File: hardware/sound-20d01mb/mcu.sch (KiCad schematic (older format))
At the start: 23 parts

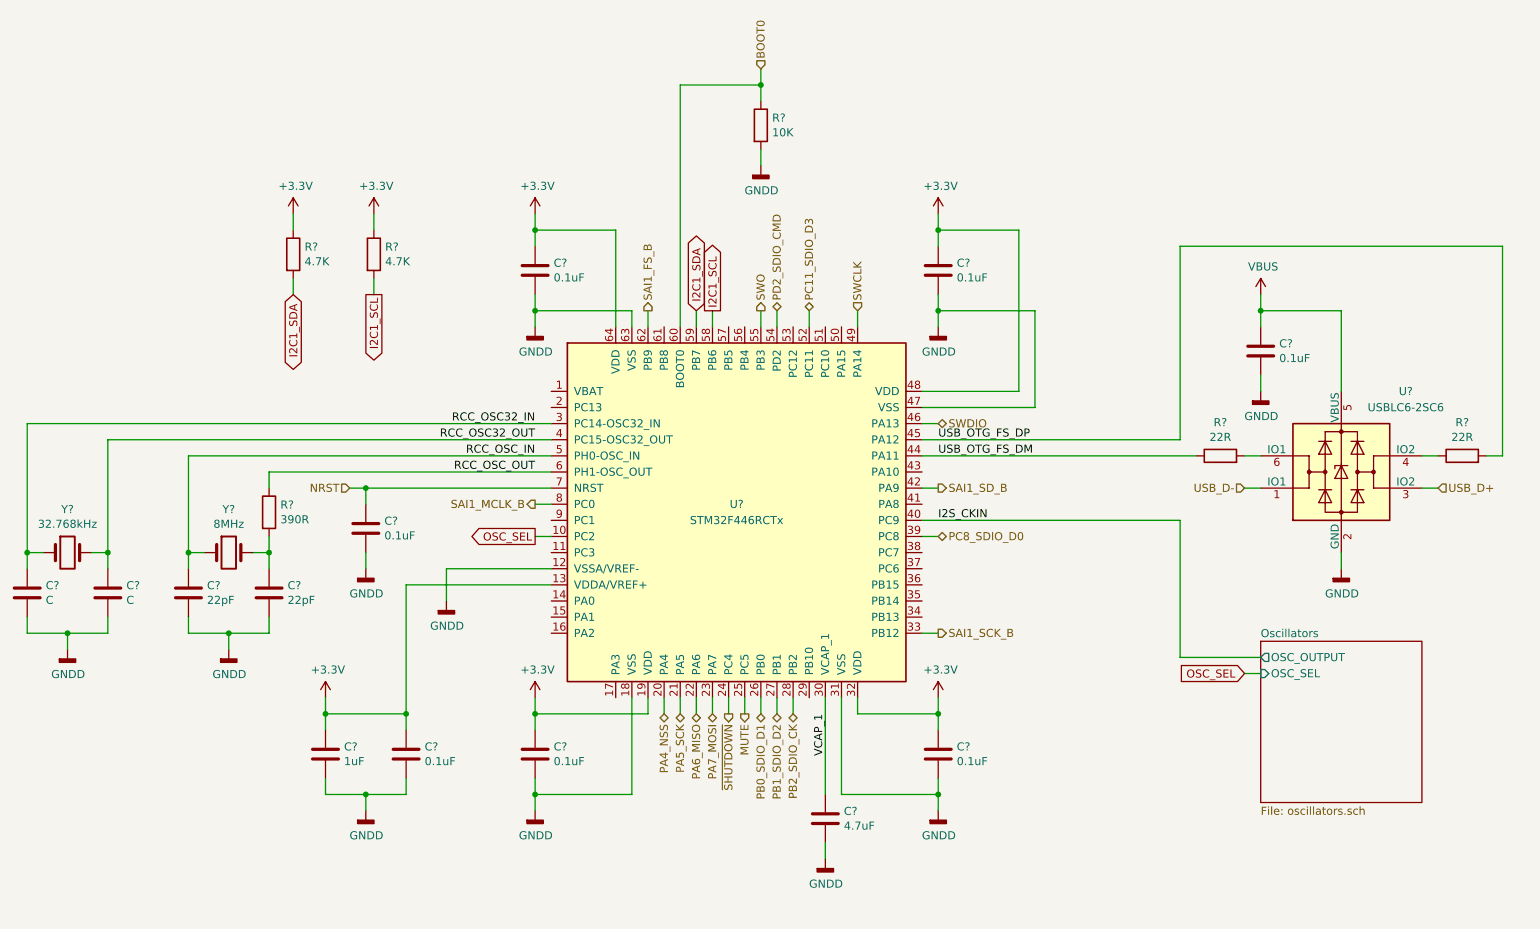
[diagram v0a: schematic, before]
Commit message: Added GPIO for MCU
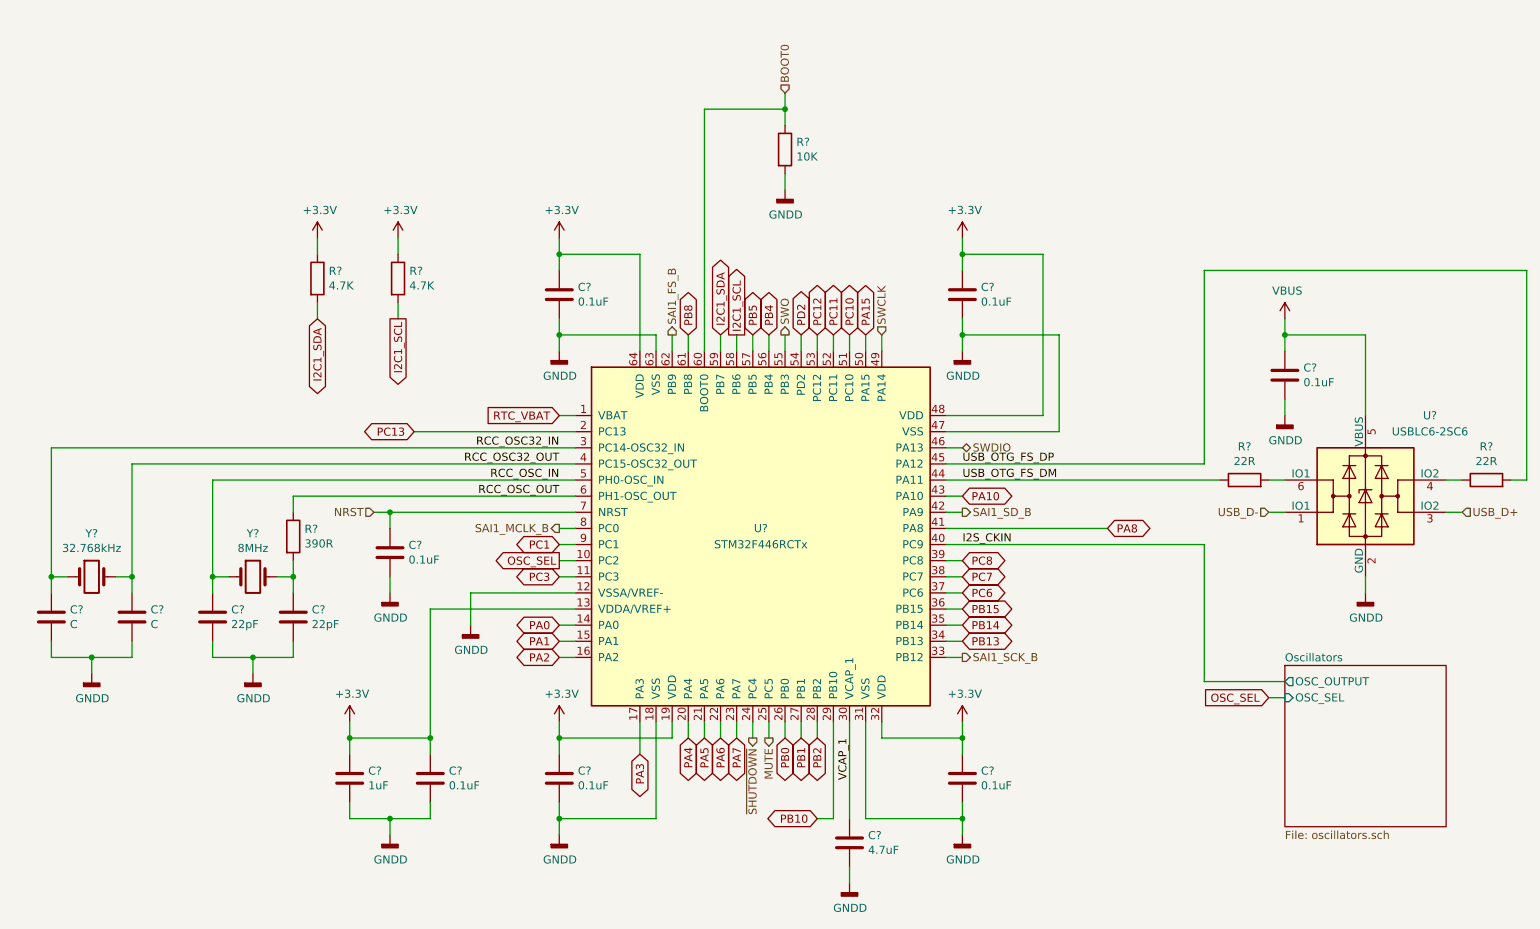
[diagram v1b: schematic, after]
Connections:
- net RTC_VBAT: now reaches U?.1 (VBAT)
- net PC3: now reaches U?.11 (PC3)
- net PA0: now reaches U?.14 (PA0)
- net PA1: now reaches U?.15 (PA1)
- net PA2: now reaches U?.16 (PA2)
- net PA3: now reaches U?.17 (PA3)
- net PC13: now reaches U?.2 (PC13)
- net PB10: now reaches U?.29 (PB10)
- net PB13: now reaches U?.34 (PB13)
- net PB14: now reaches U?.35 (PB14)
- net PB15: now reaches U?.36 (PB15)
- net PC6: now reaches U?.37 (PC6)
- net PC7: now reaches U?.38 (PC7)
- net PA8: now reaches U?.41 (PA8)
- net PA10: now reaches U?.43 (PA10)
- net PA15: now reaches U?.50 (PA15)
- net PC10: now reaches U?.51 (PC10)
- net PC12: now reaches U?.53 (PC12)
- net PB4: now reaches U?.56 (PB4)
- net PB5: now reaches U?.57 (PB5)
- net PB8: now reaches U?.61 (PB8)
- net PC1: now reaches U?.9 (PC1)
- net PA4_NSS renamed PA4
- net PA5_SCK renamed PA5
- net PA6_MISO renamed PA6
- net PA7_MOSI renamed PA7
- net PB0_SDIO_D1 renamed PB0
- net PB1_SDIO_D2 renamed PB1
- net PB2_SDIO_CK renamed PB2
- net PC11_SDIO_D3 renamed PC11
- net PC8_SDIO_D0 renamed PC8
- net PD2_SDIO_CMD renamed PD2
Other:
- moved on the sheet: C?, R?, U?, Y?

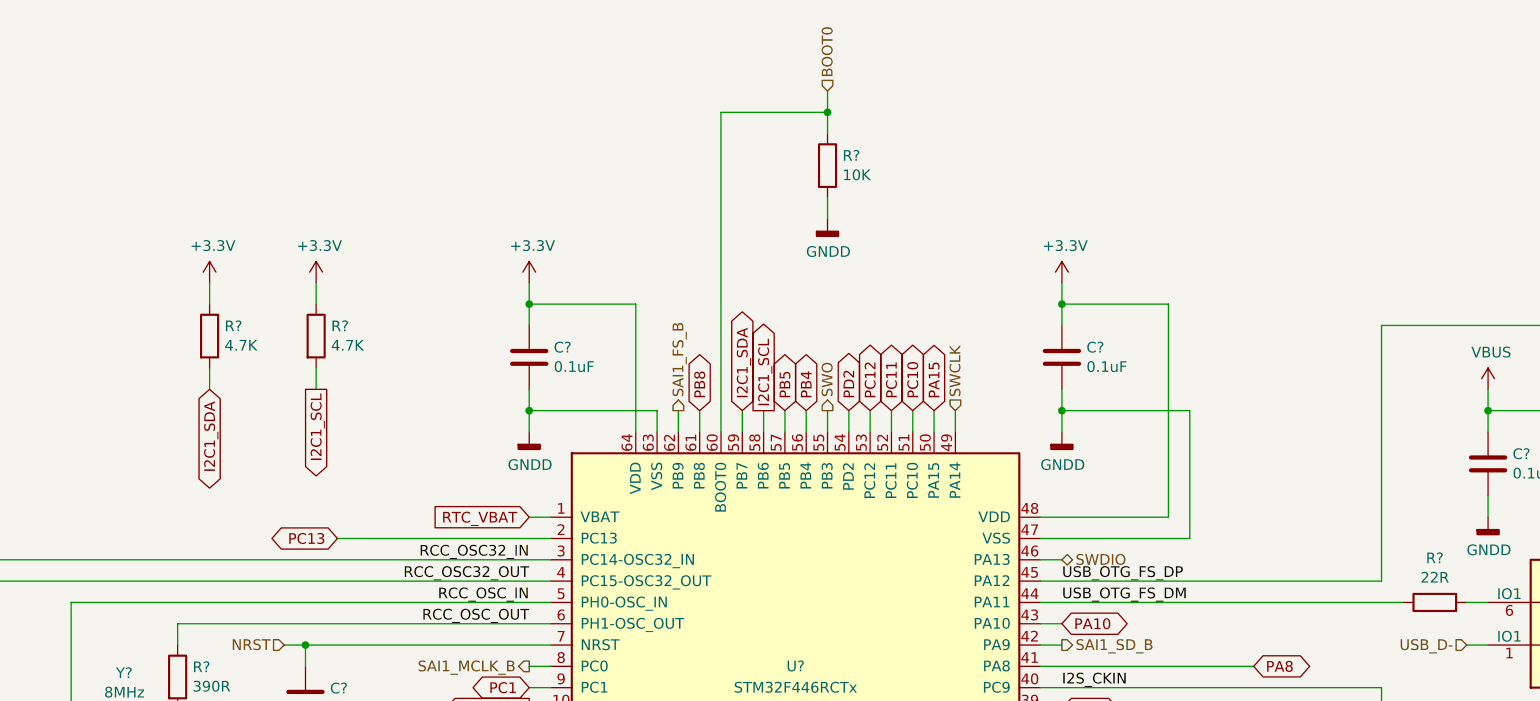
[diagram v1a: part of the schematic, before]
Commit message: Added RTC-BAT
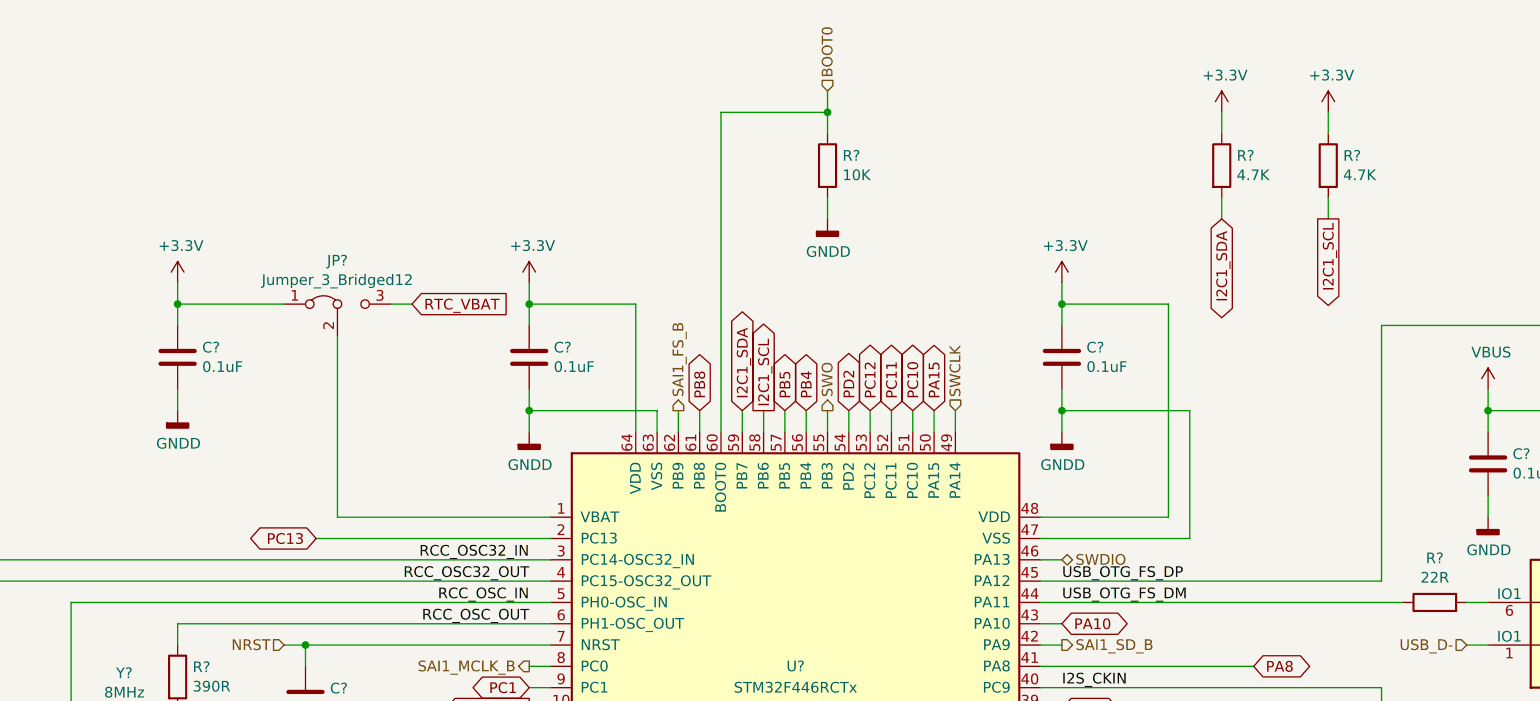
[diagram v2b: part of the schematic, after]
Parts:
- added C?: 0.1uF, Capacitor_SMD:C_1206_3216Metric_Pad1.42x1.75mm_HandSolder, symbol Device:C
- added JP?: Jumper_3_Bridged12, Connector_PinHeader_2.54mm:PinHeader_1x03_P2.54mm_Vertical, symbol Jumper:Jumper_3_Bridged12
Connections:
- net +3V3: now also C?.1, JP?.1 (A)
- net GNDD: now also C?.2
- net RTC_VBAT: now also JP?.3 (B); no longer U?.1 (VBAT)
- new net: JP?.2 (C), U?.1 (VBAT)
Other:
- moved on the sheet: R?
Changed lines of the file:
@@
 Text GLabel 5300 2550 1    50   Output ~ 0
 I2C1_SCL
-Text GLabel 2700 2450 3    50   BiDi ~ 0
+Text GLabel 7450 1650 3    50   BiDi ~ 0
 I2C1_SDA
-Text GLabel 3200 2450 3    50   Output ~ 0
+Text GLabel 7950 1650 3    50   Output ~ 0
 I2C1_SCL
 $Comp
 L Device:R R?
 U 1 1 6147BEB3
-P 2700 2200
-F 0 "R?" H 2770 2246 50  0000 L CNN
-F 1 "4.7K" H 2770 2155 50  0000 L CNN
-F 2 "Resistor_SMD:R_1206_3216Metric_Pad1.42x1.75mm_HandSolder" V 2630 2200 50  0001 C CNN
-F 3 "~" H 2700 2200 50  0001 C CNN
-	1    2700 2200
-	1    0    0    -1
-$EndComp
-Wire Wire Line
-	2700 2350 2700 2450
-Wire Wire Line
-	2700 1950 2700 2050
+P 7450 1400
+F 0 "R?" H 7520 1446 50  0000 L CNN
+F 1 "4.7K" H 7520 1355 50  0000 L CNN
+F 2 "Resistor_SMD:R_1206_3216Metric_Pad1.42x1.75mm_HandSolder" V 7380 1400 50  0001 C CNN
+F 3 "~" H 7450 1400 50  0001 C CNN
+	1    7450 1400
+	1    0    0    -1
+$EndComp
+Wire Wire Line
+	7450 1550 7450 1650
+Wire Wire Line
+	7450 1150 7450 1250
 $Comp
 L power:+3.3V #PWR?
 U 1 1 6147FF35
-P 2700 1950
-F 0 "#PWR?" H 2700 1800 50  0001 C CNN
-F 1 "+3.3V" H 2715 2123 50  0000 C CNN
-F 2 "" H 2700 1950 50  0001 C CNN
-F 3 "" H 2700 1950 50  0001 C CNN
-	1    2700 1950
+P 7450 1150
+F 0 "#PWR?" H 7450 1000 50  0001 C CNN
+F 1 "+3.3V" H 7465 1323 50  0000 C CNN
+F 2 "" H 7450 1150 50  0001 C CNN
+F 3 "" H 7450 1150 50  0001 C CNN
+	1    7450 1150
 	1    0    0    -1
 $EndComp
@@
 L Device:R R?
 U 1 1 6148000C
-P 3200 2200
-F 0 "R?" H 3270 2246 50  0000 L CNN
-F 1 "4.7K" H 3270 2155 50  0000 L CNN
-F 2 "Resistor_SMD:R_1206_3216Metric_Pad1.42x1.75mm_HandSolder" V 3130 2200 50  0001 C CNN
-F 3 "~" H 3200 2200 50  0001 C CNN
-	1    3200 2200
-	1    0    0    -1
-$EndComp
-Wire Wire Line
-	3200 2350 3200 2450
-Wire Wire Line
-	3200 1950 3200 2050
+P 7950 1400
+F 0 "R?" H 8020 1446 50  0000 L CNN
+F 1 "4.7K" H 8020 1355 50  0000 L CNN
+F 2 "Resistor_SMD:R_1206_3216Metric_Pad1.42x1.75mm_HandSolder" V 7880 1400 50  0001 C CNN
+F 3 "~" H 7950 1400 50  0001 C CNN
+	1    7950 1400
+	1    0    0    -1
+$EndComp
+Wire Wire Line
+	7950 1550 7950 1650
+Wire Wire Line
+	7950 1150 7950 1250
 $Comp
 L power:+3.3V #PWR?
 U 1 1 61480014
-P 3200 1950
-F 0 "#PWR?" H 3200 1800 50  0001 C CNN
-F 1 "+3.3V" H 3215 2123 50  0000 C CNN
-F 2 "" H 3200 1950 50  0001 C CNN
-F 3 "" H 3200 1950 50  0001 C CNN
-	1    3200 1950
+P 7950 1150
+F 0 "#PWR?" H 7950 1000 50  0001 C CNN
+F 1 "+3.3V" H 7965 1323 50  0000 C CNN
+F 2 "" H 7950 1150 50  0001 C CNN
+F 3 "" H 7950 1150 50  0001 C CNN
+	1    7950 1150
 	1    0    0    -1
 $EndComp
@@
 Wire Wire Line
 	7300 3150 7300 2550
-Text GLabel 4200 3050 0    50   Input ~ 0
+Text GLabel 3650 2050 2    50   Input ~ 0
 RTC_VBAT
-Wire Wire Line
-	4300 3050 4200 3050
-Text GLabel 3300 3150 0    50   BiDi ~ 0
+Text GLabel 3200 3150 0    50   BiDi ~ 0
 PC13
 Text GLabel 4200 3850 0    50   BiDi ~ 0
@@
 Wire Wire Line
 	4700 4950 4700 5150
-Wire Wire Line
-	3300 3150 4300 3150
 Text GLabel 5000 5050 3    50   BiDi ~ 0
 PA4
@@
 Wire Wire Line
 	5000 2650 5000 2550
+$Comp
+L Device:C C?
+U 1 1 61966FEF
+P 2550 2300
+F 0 "C?" H 2665 2346 50  0000 L CNN
+F 1 "0.1uF" H 2665 2255 50  0000 L CNN
+F 2 "Capacitor_SMD:C_1206_3216Metric_Pad1.42x1.75mm_HandSolder" H 2588 2150 50  0001 C CNN
+F 3 "~" H 2550 2300 50  0001 C CNN
+	1    2550 2300
+	1    0    0    -1
+$EndComp
+$Comp
+L power:GNDD #PWR?
+U 1 1 61967133
+P 2550 2550
+F 0 "#PWR?" H 2550 2300 50  0001 C CNN
+F 1 "GNDD" H 2554 2395 50  0000 C CNN
+F 2 "" H 2550 2550 50  0001 C CNN
+F 3 "" H 2550 2550 50  0001 C CNN
+	1    2550 2550
+	1    0    0    -1
+$EndComp
+$Comp
+L power:+3.3V #PWR?
+U 1 1 6197B6FC
+P 2550 1950
+F 0 "#PWR?" H 2550 1800 50  0001 C CNN
+F 1 "+3.3V" H 2565 2123 50  0000 C CNN
+F 2 "" H 2550 1950 50  0001 C CNN
+F 3 "" H 2550 1950 50  0001 C CNN
+	1    2550 1950
+	1    0    0    -1
+$EndComp
+Wire Wire Line
+	2550 2050 3050 2050
+$Comp
+L Jumper:Jumper_3_Bridged12 JP?
+U 1 1 61A3432C
+P 3300 2050
+F 0 "JP?" H 3300 2254 50  0000 C CNN
+F 1 "Jumper_3_Bridged12" H 3300 2163 50  0000 C CNN
+F 2 "Connector_PinHeader_2.54mm:PinHeader_1x03_P2.54mm_Vertical" H 3300 2050 50  0001 C CNN
+F 3 "~" H 3300 2050 50  0001 C CNN
+	1    3300 2050
+	1    0    0    -1
+$EndComp
+Wire Wire Line
+	2550 1950 2550 2050
+Connection ~ 2550 2050
+Wire Wire Line
+	2550 2050 2550 2150
+Wire Wire Line
+	3550 2050 3650 2050
+Wire Wire Line
+	2550 2450 2550 2550
+Wire Wire Line
+	4300 3050 3300 3050
+Wire Wire Line
+	4300 3150 3200 3150
+Wire Wire Line
+	3300 3050 3300 2200
 $EndSCHEMATC

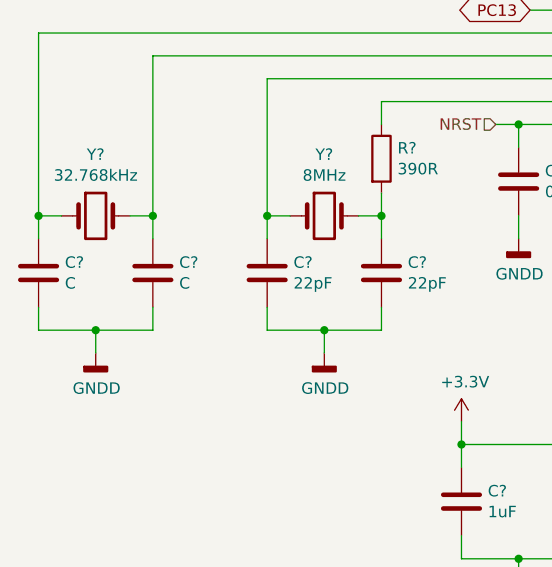
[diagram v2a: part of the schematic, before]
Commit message: Load capacitance for RTC Crystal
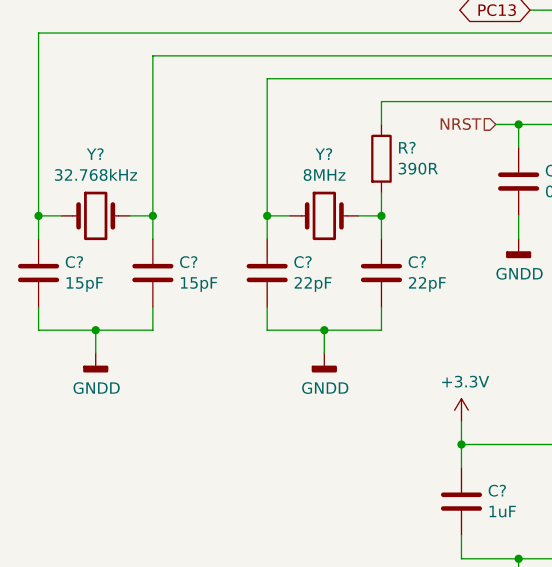
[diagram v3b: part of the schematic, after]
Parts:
- C? (x2): value C -> 15pF
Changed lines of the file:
@@
 P 1050 4300
 F 0 "C?" H 1165 4346 50  0000 L CNN
-F 1 "C" H 1165 4255 50  0000 L CNN
+F 1 "15pF" H 1165 4255 50  0000 L CNN
 F 2 "Capacitor_SMD:C_1206_3216Metric_Pad1.42x1.75mm_HandSolder" H 1088 4150 50  0001 C CNN
 F 3 "~" H 1050 4300 50  0001 C CNN
@@
 P 1550 4300
 F 0 "C?" H 1665 4346 50  0000 L CNN
-F 1 "C" H 1665 4255 50  0000 L CNN
+F 1 "15pF" H 1665 4255 50  0000 L CNN
 F 2 "Capacitor_SMD:C_1206_3216Metric_Pad1.42x1.75mm_HandSolder" H 1588 4150 50  0001 C CNN
 F 3 "~" H 1550 4300 50  0001 C CNN

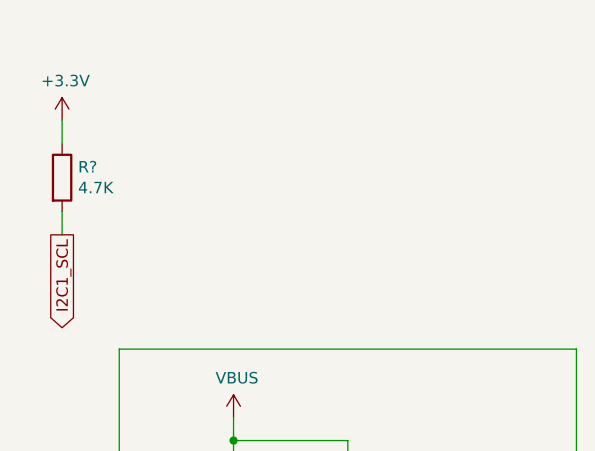
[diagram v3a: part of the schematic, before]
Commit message: Added connector for I2C
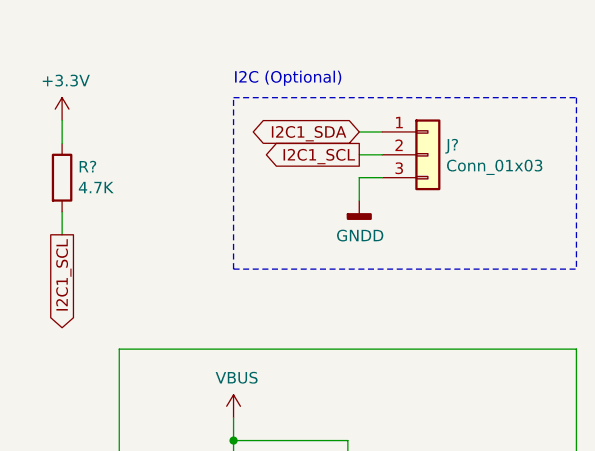
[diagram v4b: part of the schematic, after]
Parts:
- added J?: Conn_01x03, Connector_PinHeader_2.54mm:PinHeader_1x03_P2.54mm_Vertical, symbol Connector_Generic:Conn_01x03
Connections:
- net GNDD: now also J?.3 (Pin_3)
- net I2C1_SCL: now also J?.2 (Pin_2)
- net I2C1_SDA: now also J?.1 (Pin_1)
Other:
- note added: "I2C (Optional)"
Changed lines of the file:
@@
 Wire Wire Line
 	3300 3050 3300 2200
+Text GLabel 9250 1200 0    50   BiDi ~ 0
+I2C1_SDA
+Text GLabel 9250 1300 0    50   Output ~ 0
+I2C1_SCL
+$Comp
+L power:GNDD #PWR?
+U 1 1 61A1F060
+P 9250 1500
+F 0 "#PWR?" H 9250 1250 50  0001 C CNN
+F 1 "GNDD" H 9254 1345 50  0000 C CNN
+F 2 "" H 9250 1500 50  0001 C CNN
+F 3 "" H 9250 1500 50  0001 C CNN
+	1    9250 1500
+	1    0    0    -1
+$EndComp
+$Comp
+L Connector_Generic:Conn_01x03 J?
+U 1 1 61A1F1F2
+P 9550 1300
+F 0 "J?" H 9630 1342 50  0000 L CNN
+F 1 "Conn_01x03" H 9630 1251 50  0000 L CNN
+F 2 "Connector_PinHeader_2.54mm:PinHeader_1x03_P2.54mm_Vertical" H 9550 1300 50  0001 C CNN
+F 3 "~" H 9550 1300 50  0001 C CNN
+	1    9550 1300
+	1    0    0    -1
+$EndComp
+Wire Wire Line
+	9350 1200 9250 1200
+Wire Wire Line
+	9350 1300 9250 1300
+Wire Wire Line
+	9350 1400 9250 1400
+Wire Wire Line
+	9250 1400 9250 1500
+Text Notes 8700 1000 0    50   ~ 0
+I2C (Optional)
+Wire Notes Line
+	8700 1050 10200 1050
+Wire Notes Line
+	8700 1800 10200 1800
+Wire Notes Line
+	10200 1050 10200 1800
+Wire Notes Line
+	8700 1800 8700 1050
 $EndSCHEMATC
